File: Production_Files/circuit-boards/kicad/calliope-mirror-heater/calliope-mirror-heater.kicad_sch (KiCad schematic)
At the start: 37 parts, among them J101 Conn_02x15_Odd_Even, J102 USB_C_Receptacle_USB2.0_16P, SW102 select-heater-power-source, U102 LM358DR2G, U104 TP5709S5, U105 GAQY212GSX, U401 XC6206P332MR-G

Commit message: Electrically done
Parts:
- removed C402: 1u/25V, Capacitor_SMD:C_0402_1005Metric, symbol Device:C_Small
- added C103: 22u/25V, Capacitor_SMD:C_0805_2012Metric, symbol Device:C_Small
- added D106, D1904: H3V3L10B, Diode_SMD:D_SOD-882D, symbol Device:D_TVS_Small
- added D109, D1905: H5VL10B, Diode_SMD:D_SOD-882D, symbol Device:D_TVS_Small
- added TP105, TP106, TP107, TP108, TP109, TP110, TP111, TP112, TP113, TP114, TP115, TP116, TP117, TP118, TP119, TP120, TP121, TP122, TP123, TP124, TP125, TP126, TP127, TP128, TP129: TestPoint_Small, testpoint_solid-zone-connection_lib:TestPoint_Pad_D1.0mm, symbol Connector:TestPoint_Small
- C101: value C_Small -> 100n/16V; footprint (none) -> Capacitor_SMD:C_0402_1005Metric; LCSC (none) -> C1525
- C102: value 100n/3.3V -> 100n/16V; footprint (none) -> Capacitor_SMD:C_0402_1005Metric; LCSC (none) -> C1525
- D103, D104: footprint (none) -> LED_SMD:LED_0805_2012Metric; LCSC (none) -> C2296
- J101: LCSC (none) -> C18198029
- R101: value Heater-trace_16R_length-6.2m_width-0.2mm -> Heater-trace_16R_length-6m_width-0.2mm; footprint (none) -> TestPoint:TestPoint_2Pads_Pitch5.08mm_Drill1.3mm
- R103, R108: footprint Resistor_SMD:R_0603_1608Metric -> Resistor_SMD:R_0402_1005Metric; LCSC C23186 -> C25905
- SW102: footprint (none) -> dpdt-slide-switch:SW_DPDT_shou-han_MST-22D18G2-BD-125
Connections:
- net +3.3V: now also D1904.2 (A2), TP115.1, TP128.1
- net +5V_USB: now also TP105.1
- net GND: now also C103.2, D106.1 (A1), D109.1 (A1), D1904.1 (A1), D1905.1 (A1), TP106.1, TP111.1, TP116.1, TP127.1, TP129.1
- net calliope_M0+: now also TP123.1
- net calliope_M0-: now also TP122.1
- net calliope_P0: now also D106.2 (A2)
- net at D107.1 (K), D108.1 (K), R107.1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: now also TP109.1
- net at R102.1, TH101.2, U102.3 (+): now also TP114.1
- net at R110.2, R111.2, U104.3 (Out)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: now also TP110.1
- net at D103.1 (K), D104.2 (A), R109.2: now also D109.2 (A2), TP121.1
- net at D103.2 (A), D104.1 (K), R101.2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: now also D1905.2 (A2), TP113.1
- net at SW102.2 (B), U105.4: now also TP112.1, TP124.1
- net at D105.1 (K), SW102.3 (C): now also TP126.1
- net at R101.1, R109.1, SW102.5 (B): now also TP120.1, TP125.1
- net at C102.1, R107.2, U104.5 (VDD): now also TP108.1
- net at R105.1, U104.1 (SET): now also TP107.1
- net at C401.1, D102.1 (K), TP401.1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: now also C103.1
- net USB_DP: now reaches J102.A6 (D+), J102.B6 (D+), TP104.1
- net USB_DN: now reaches J102.A7 (D-), J102.B7 (D-), TP103.1
- net at U102.5 (+): now also TP118.1
- net at U102.6 (-): now also TP119.1
- net at U102.7: now also TP117.1
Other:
- note added: "2 big MLCCs is better than one big and one small"
- note added: "3.3V"
- note added: "5V"
- note added: "Heater trace: Actual trace now: Trace of 0.2 mm on both sides (1 oz/sqft Cu), total length 5916 mm. R at 25°C is 14.4 Ohms, R at 80°C is 17.4 Ohms."
- note added: "TVS here because it is so exposed to the touch"
- note added: "This NTC has 100k at 25°C, and R falls when heated. "B constant 25-80°C" is 4303K. Or use lookup table from datasheet (Search for "NCP15WF104D"). 127.1k@20°C,100k@25°C,50.7k@40°C,22.2k@60°C,10.5k@80°C."
- note added: "Unused. Nets labeled to enable differential routing"
- note removed: "Add 3.3v tvs"
- note removed: "This NTC has 100k at 25°C. B constant 25-80°C is 4303K. Or use lookup table from datasheet."
- moved on the sheet: TP103, TP104

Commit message: Finished calliope board! Ready to export production files.
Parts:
- renumbered C401 to C1, C102 to C2, C103 to C3, C405 to C4, C101 to C5, D1904 to D1, D103 to D10, D109 to D11, D106 to D2, D101 to D3, D102 to D4, D107 to D5, D108 to D6, D105 to D7, D1905 to D8, D104 to D9, J102 to J1, J101 to J2, R103 to R1, R109 to R10, R108 to R2, R102 to R3, R105 to R4, R106 to R5, R107 to R6, R110 to R7, R111 to R8, R101 to R9, SW102 to SW1, TH101 to TH1, TP106 to TP1, TP401 to TP10, TP108 to TP11, TP107 to TP12, TP402 to TP13, TP403 to TP14, TP109 to TP15, TP110 to TP16, TP111 to TP17, TP118 to TP18, TP119 to TP19, TP101 to TP2, TP112 to TP20, TP113 to TP21, TP117 to TP22, TP123 to TP23, TP124 to TP24, TP126 to TP25, TP122 to TP26, TP125 to TP27, TP127 to TP28, TP121 to TP29, TP102 to TP3, TP128 to TP30, TP129 to TP31, TP120 to TP32, TP103 to TP4, TP104 to TP5, TP105 to TP6, TP115 to TP7, TP116 to TP8, TP114 to TP9, U102 to U1, U104 to U2, U401 to U3, U105 to U4
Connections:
- net GND: now also J2.30 (Pin_30)
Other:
- company: (none) -> openUC2 GmbH
- title: (none) -> calliope-mirror-heater

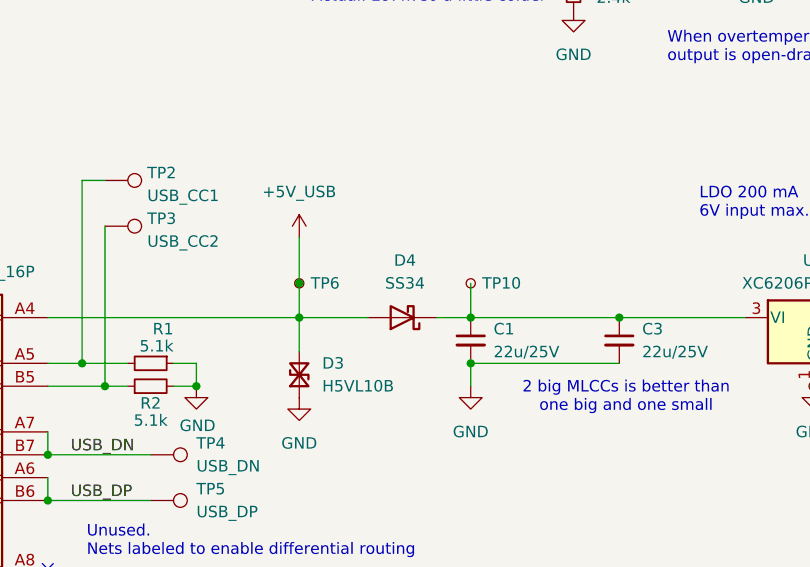
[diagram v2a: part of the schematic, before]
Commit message: Finished Rev B: correct slide-switch fp
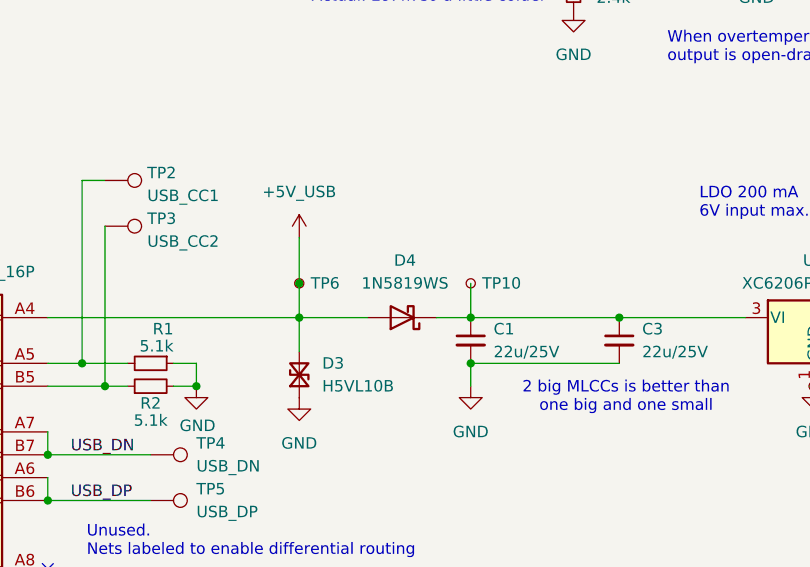
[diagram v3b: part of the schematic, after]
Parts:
- removed D4: SS34, Diode_SMD:D_SMA, symbol Diode:SS34
- added D4: 1N5819WS, Diode_SMD:D_SOD-323, symbol Diode:1N5819WS
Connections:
- net +5V_USB: now also D4.2 (A)
- net at C1.1, C3.1, TP10.1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: now also D4.1 (K)
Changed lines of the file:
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@@
 		(title "calliope-mirror-heater")
 		(date "2025-09-22")
-		(rev "A")
+		(rev "B")
 		(company "openUC2 GmbH")
 		(comment 1 "christiankuttke")
@@
 	)
 	(symbol
+		(lib_id "Diode:1N5819WS")
+		(at 95.25 152.4 180)
+		(unit 1)
+		(exclude_from_sim no)
+		(in_bom yes)
+		(on_board yes)
+		(dnp no)
+		(fields_autoplaced yes)
+		(property "Reference" "D4"
+			(at 95.5675 146.05 0)
+			(effects
+				(font
+					(size 1.27 1.27)
+				)
+			)
+		)
+		(property "Value" "1N5819WS"
+			(at 95.5675 148.59 0)
+			(effects
+				(font
+					(size 1.27 1.27)
+				)
+			)
+		)
+		(property "Footprint" "Diode_SMD:D_SOD-323"
+			(at 95.25 147.955 0)
+			(effects
+				(font
+					(size 1.27 1.27)
+				)
+				(hide yes)
+			)
+		)
+		(property "Datasheet" "https://datasheet.lcsc.com/lcsc/2204281430_Guangdong-Hottech-1N5819WS_C191023.pdf"
+			(at 95.25 152.4 0)
+			(effects
+				(font
+					(size 1.27 1.27)
+				)
+				(hide yes)
+			)
+		)
+		(property "Description" "40V 600mV@1A 1A SOD-323 Schottky Barrier Diodes, SOD-323"
+			(at 95.25 152.4 0)
+			(effects
+				(font
+					(size 1.27 1.27)
+				)
+				(hide yes)
+			)
+		)
+		(property "LCSC" "C191023"
+			(at 95.25 152.4 0)
+			(effects
+				(font
+					(size 1.27 1.27)
+				)
+				(hide yes)
+			)
+		)
+		(pin "2"
+		)
+		(pin "1"
+		)
+		(instances
+			(project ""
+				(path "/8fbd14f2-33ba-4b40-9234-9218c55a9a3e"
+					(reference "D4")
+					(unit 1)
+				)
+			)
+		)
+	)
+	(symbol
 		(lib_id "Device:LED_Small")
 		(at 241.3 130.81 180)
@@
 					(unit 1)
 				)
-			)
-		)
-	)
-	(symbol
-		(lib_id "Diode:SS34")
-		(at 95.25 152.4 180)
-		(unit 1)
-		(exclude_from_sim no)
-		(in_bom yes)
-		(on_board yes)
-		(dnp no)
-		(fields_autoplaced yes)
-		(property "Reference" "D4"
-			(at 95.5675 146.05 0)
-			(effects
-				(font
-					(size 1.27 1.27)
-				)
-			)
-		)
-		(property "Value" "SS34"
-			(at 95.5675 148.59 0)
-			(effects
-				(font
-					(size 1.27 1.27)
-				)
-			)
-		)
-		(property "Footprint" "Diode_SMD:D_SMA"
-			(at 95.25 147.955 0)
-			(effects
-				(font
-					(size 1.27 1.27)
-				)
-				(hide yes)
-			)
-		)
-		(property "Datasheet" "https://www.vishay.com/docs/88751/ss32.pdf"
-			(at 95.25 152.4 0)
-			(effects
-				(font
-					(size 1.27 1.27)
-				)
-				(hide yes)
-			)
-		)
-		(property "Description" "40V 3A Schottky Diode, SMA"
-			(at 95.25 152.4 0)
-			(effects
-				(font
-					(size 1.27 1.27)
-				)
-				(hide yes)
-			)
-		)
-		(property "LCSC" "C8678"
-			(at 95.25 152.4 0)
-			(effects
-				(font
-					(size 1.27 1.27)
-				)
-				(hide yes)
-			)
-		)
-		(pin "2"
-		)
-		(pin "1"
-		)
-		(instances
-			(project ""
-				(path "/8fbd14f2-33ba-4b40-9234-9218c55a9a3e"
-					(reference "D4")
-					(unit 1)
-				)
